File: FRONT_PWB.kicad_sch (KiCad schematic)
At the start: 26 parts, among them IC401 74AHC273, Q401 2SD1664, Q402 2SD1664

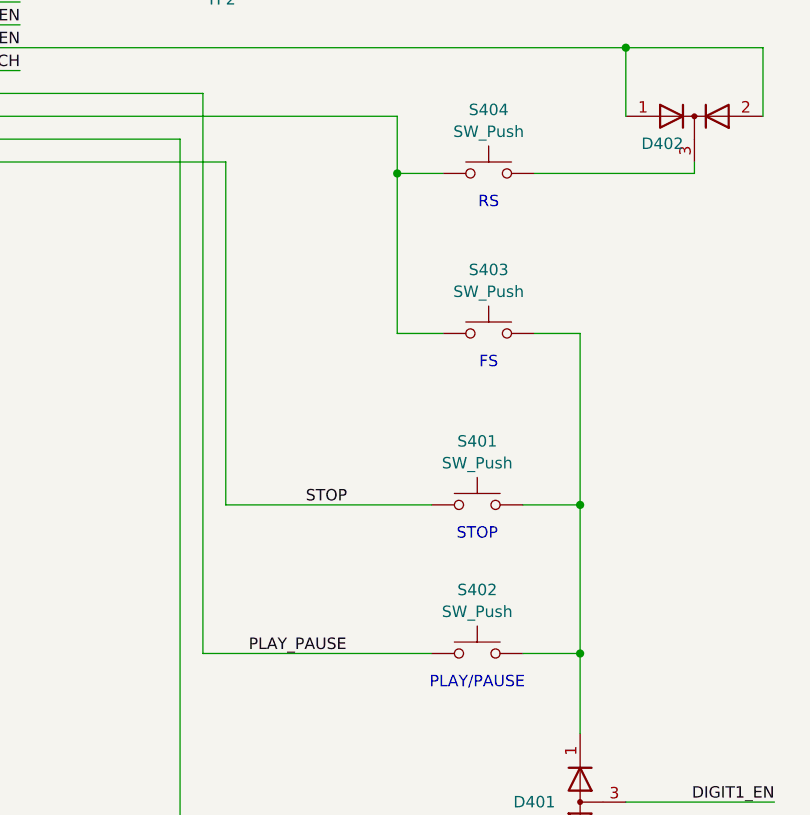
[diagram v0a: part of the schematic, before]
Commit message: Small update, some typo fixes, more comments added to help understanding
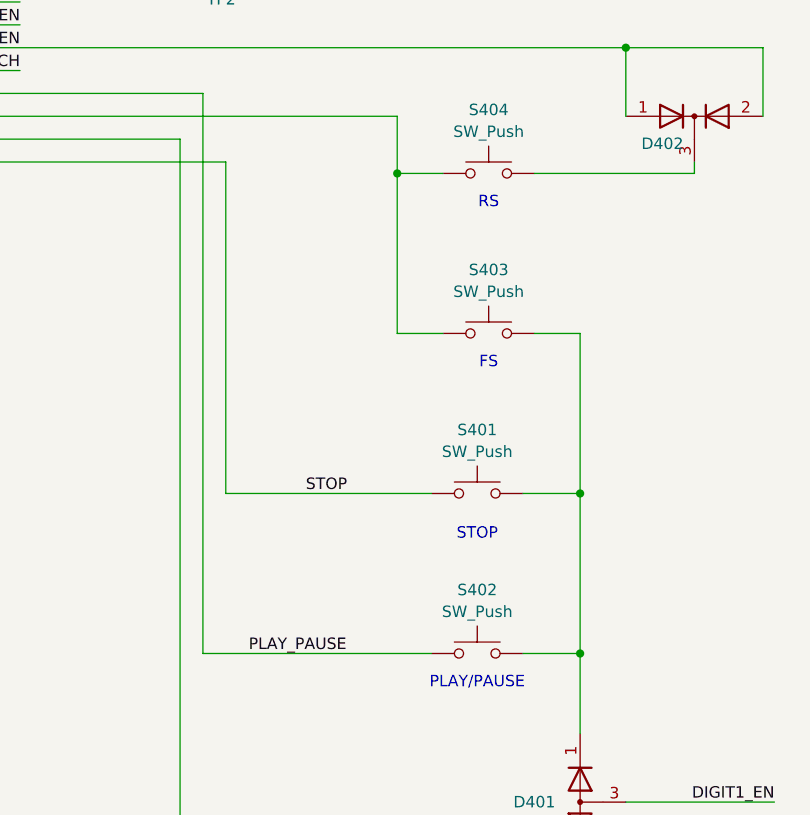
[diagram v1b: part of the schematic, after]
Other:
- moved on the sheet: S401
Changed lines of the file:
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@@
 	)
 	(junction
-		(at 119.38 113.03)
+		(at 119.38 111.76)
 		(diameter 0)
 		(color 0 0 0 0)
@@
 	(wire
 		(pts
-			(xy 119.38 113.03) (xy 119.38 129.54)
+			(xy 119.38 111.76) (xy 119.38 129.54)
 		)
 		(stroke
@@
 	(wire
 		(pts
-			(xy 119.38 93.98) (xy 119.38 113.03)
+			(xy 119.38 93.98) (xy 119.38 111.76)
 		)
 		(stroke
@@
 	(wire
 		(pts
-			(xy 80.01 113.03) (xy 102.87 113.03)
+			(xy 80.01 111.76) (xy 102.87 111.76)
 		)
 		(stroke
@@
 	(wire
 		(pts
-			(xy 119.38 113.03) (xy 113.03 113.03)
-		)
-		(stroke
-			(width 0)
-			(type default)
-		)
-	)
-	(wire
-		(pts
-			(xy 80.01 74.93) (xy 80.01 113.03)
+			(xy 119.38 111.76) (xy 113.03 111.76)
+		)
+		(stroke
+			(width 0)
+			(type default)
+		)
+	)
+	(wire
+		(pts
+			(xy 80.01 74.93) (xy 80.01 111.76)
 		)
 		(stroke
@@
 	)
 	(label "STOP"
-		(at 88.9 113.03 0)
+		(at 88.9 111.76 0)
 		(fields_autoplaced yes)
 		(effects
@@
 	(symbol
 		(lib_id "Switch:SW_Push")
-		(at 107.95 113.03 0)
+		(at 107.95 111.76 0)
 		(unit 1)
 		(exclude_from_sim no)
@@
 		(fields_autoplaced yes)
 		(property "Reference" "S401"
-			(at 107.95 105.9645 0)
+			(at 107.95 104.6945 0)
 			(effects
 				(font
@@
 		)
 		(property "Value" "SW_Push"
-			(at 107.95 108.3888 0)
+			(at 107.95 107.1188 0)
 			(effects
 				(font
@@
 		)
 		(property "Footprint" "Button_Switch_THT:SW_PUSH_6mm_H4.3mm"
-			(at 107.95 107.95 0)
+			(at 107.95 106.68 0)
 			(effects
 				(font
@@
 		)
 		(property "Datasheet" "~"
-			(at 107.95 107.95 0)
+			(at 107.95 106.68 0)
 			(effects
 				(font
@@
 		)
 		(property "Description" "Push button switch, generic, two pins"
-			(at 107.95 113.03 0)
-			(effects
-				(font
+			(at 107.95 111.76 0)
+			(effects
+				(font
